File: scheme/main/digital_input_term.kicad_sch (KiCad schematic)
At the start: 1 part, among them X1 DG141V-2.54-08P

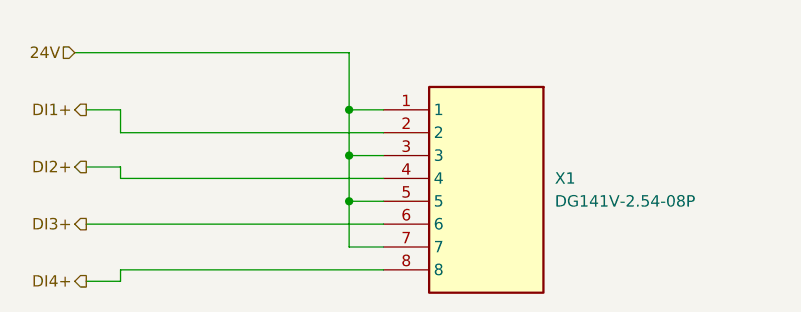
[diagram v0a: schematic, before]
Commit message: toplevel layout, can bus
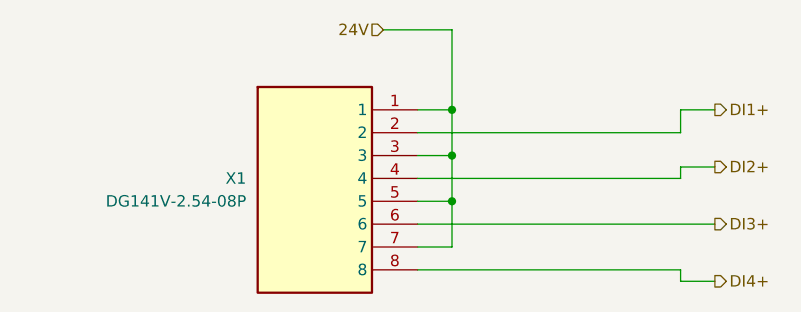
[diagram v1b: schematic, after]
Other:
- moved on the sheet: X1

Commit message: sheets titles
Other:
- title: (none) -> Клеммник цифровых входов
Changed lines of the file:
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@@
 	(generator_version "8.0")
 	(paper "A4")
+	(title_block
+		(title "Клеммник цифровых входов")
+	)
 	(junction
 		(at 160.02 90.17)
